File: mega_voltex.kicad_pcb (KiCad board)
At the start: 2 copper layers, 170 x 115 mm, 46 parts, among them J6 HEADER_2, J7 HEADER_7, J8 HEADER_5, J9 Arduino_Mega_Header, Q1 MMBT2222AWT1G, Q2 MMBT2222AWT1G, Q3 MMBT2222AWT1G

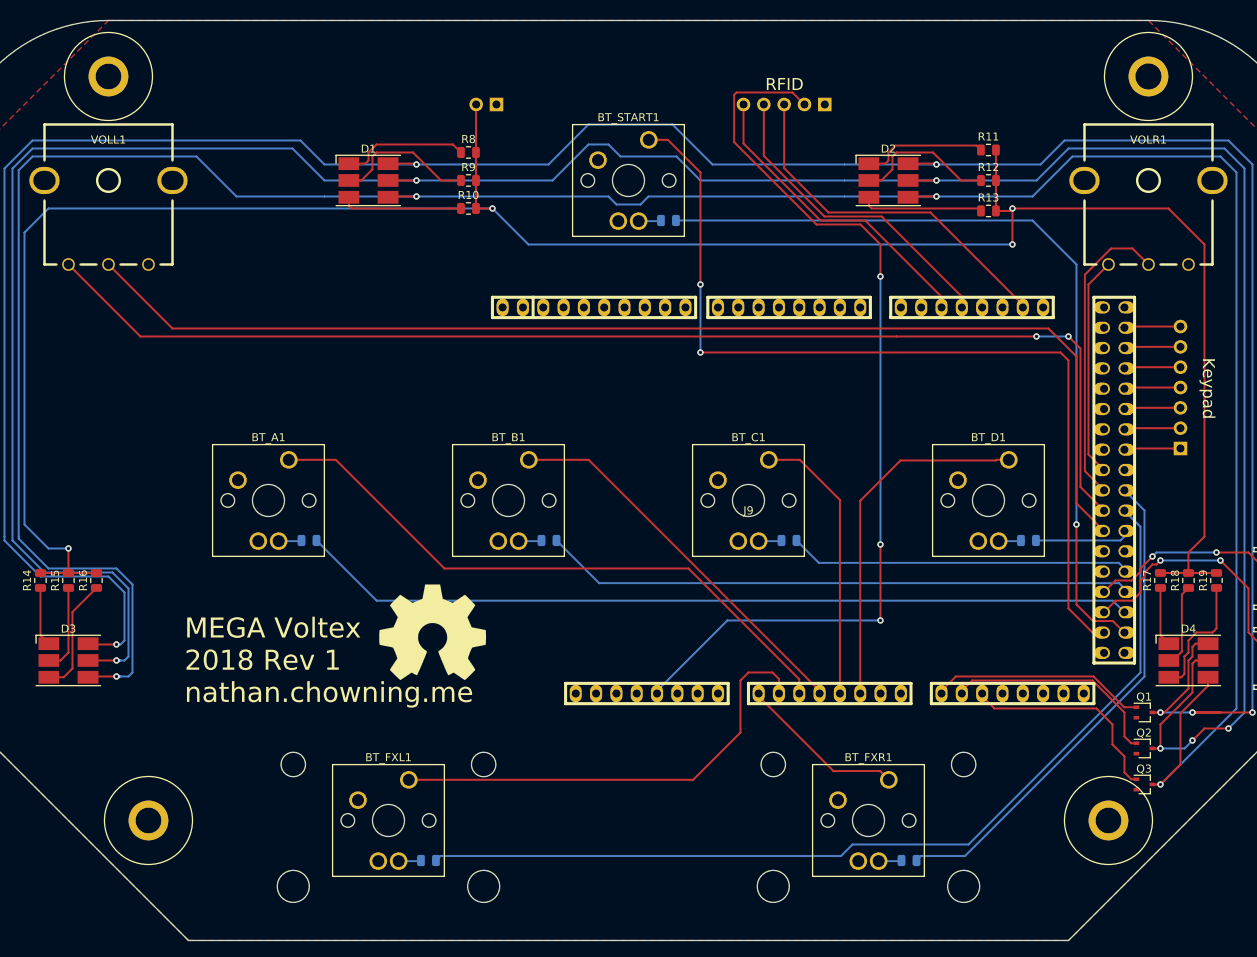
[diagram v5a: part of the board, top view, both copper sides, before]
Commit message: Added maxima silkscreen & moved top mounting holes
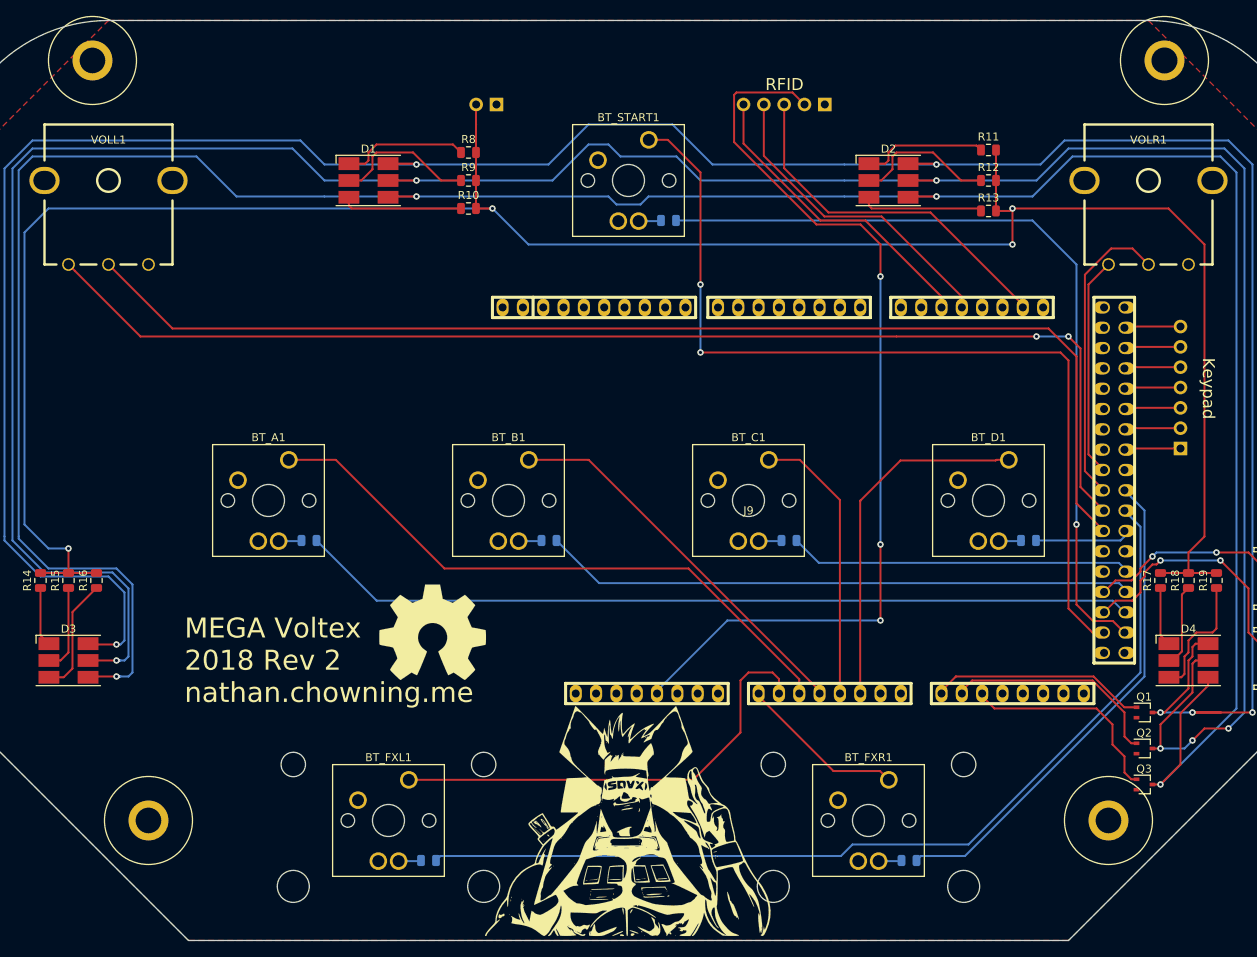
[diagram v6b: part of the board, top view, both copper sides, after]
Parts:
- added G***: LOGO, mega_voltex:maxima, F.Cu at (110.5, 125.0)
- moved Mounting Hole 2.83 mm to (43.0, 30.0)
- moved REF** 2.83 mm to (177.0, 30.0)
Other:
- board text added: "MEGA Voltex 2018 Rev 2 nathan.chowning.me"
- board text removed: "MEGA Voltex 2018 Rev 1 nathan.chowning.me"
